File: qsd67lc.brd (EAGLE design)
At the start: 71.1 x 100 mm, 67 parts, among them CON1 RIA-AKL-230-04, CON2 RIA-AKL-230-04, CON3 RIA-AKL-230-03, IC1 MEGA8-P, IC2 BTS555E3146, IC3 MAX3232CPE, IC4 LM2576S, IC5 FT232RL, IC6 ISO7221A, Q1 16MHz, T1 BCR141, U1 HC_05, X2 RS232

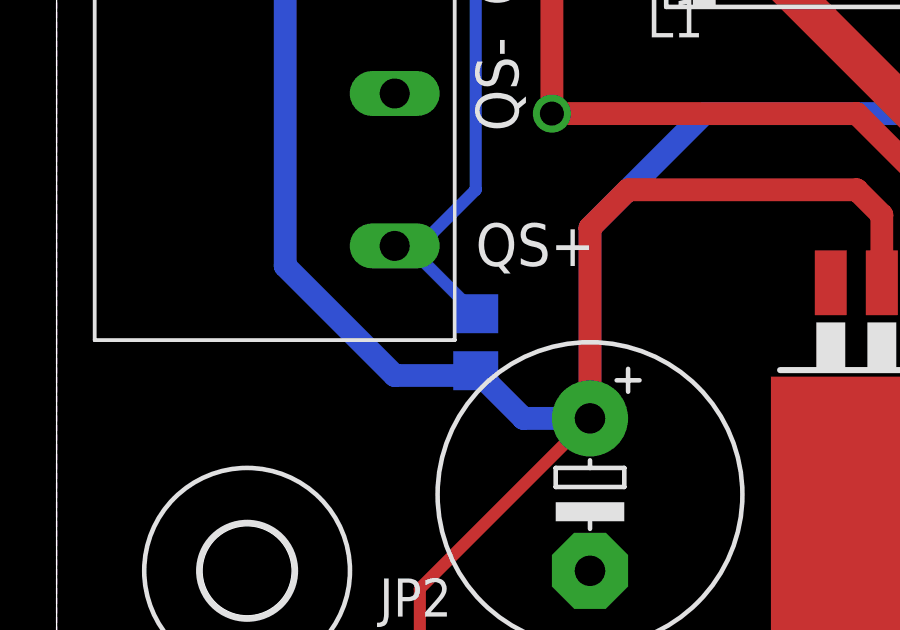
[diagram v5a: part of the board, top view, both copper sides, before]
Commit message: removed doubled pullup resistor for QS+ (R14)
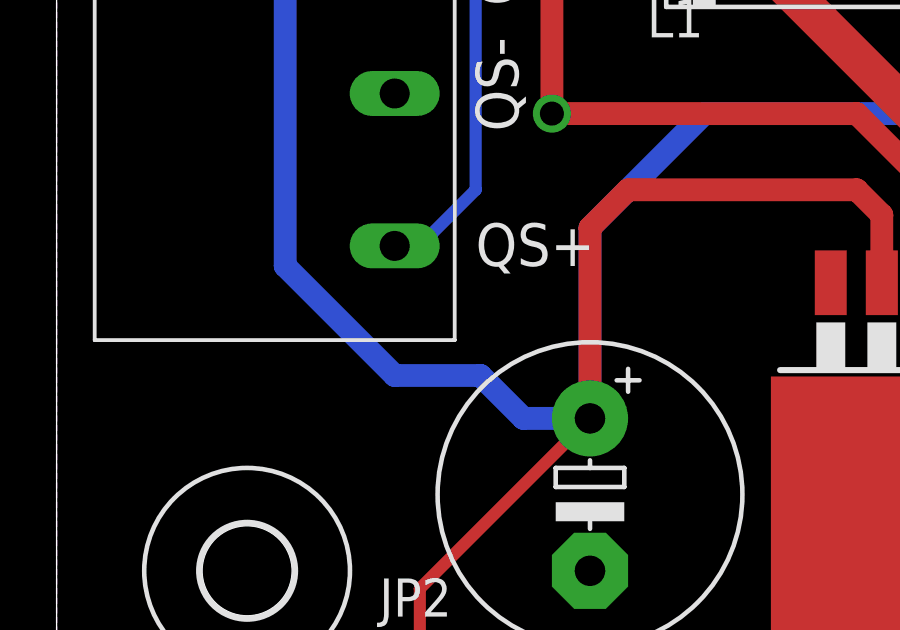
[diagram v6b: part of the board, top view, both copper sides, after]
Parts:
- removed R14: 10k, rcl:R0805
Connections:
- net +3V3: no longer R14.2
- net QS+: no longer R14.1
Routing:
- net QS+: track 40.5 -> 37.3 mm
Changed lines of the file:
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@@
 <?xml version="1.0" encoding="utf-8"?>
 <!DOCTYPE eagle SYSTEM "eagle.dtd">
-<eagle version="9.2.1">
+<eagle version="9.5.0">
 <drawing>
 <settings>
@@
 <attribute name="VALUE" x="69.85" y="13.97" size="1.27" layer="27" rot="R90"/>
 </element>
-<element name="R14" library="rcl" library_urn="urn:adsk.eagle:library:334" package="R0805" package3d_urn="urn:adsk.eagle:package:23553/2" value="10k" x="13.97" y="13.97" smashed="yes" rot="MR270">
-<attribute name="NAME" x="12.7" y="14.605" size="1.27" layer="26" rot="MR270"/>
-<attribute name="SPICEPREFIX" value="R" x="13.97" y="13.97" size="1.778" layer="28" rot="MR270" display="off"/>
-<attribute name="VALUE" x="16.51" y="14.605" size="1.27" layer="28" rot="MR270"/>
-</element>
 <element name="C19" library="rcl" library_urn="urn:adsk.eagle:library:334" package="C0805" package3d_urn="urn:adsk.eagle:package:23617/2" value="100nF" x="36.83" y="41.91" smashed="yes" rot="MR90">
 <attribute name="NAME" x="38.1" y="40.64" size="1.27" layer="26" rot="MR90"/>
@@
 <contactref element="JP4" pad="1"/>
 <contactref element="CON3" pad="P$2"/>
-<wire x1="65.07" y1="70.9" x2="67.31" y2="93.66" width="0" layer="19" extent="1-1"/>
-<wire x1="63.82" y1="69.15" x2="65.07" y2="70.9" width="0" layer="19" extent="1-1"/>
-<wire x1="56.2" y1="66.04" x2="63.82" y2="69.15" width="0" layer="19" extent="1-1"/>
-<wire x1="53.34" y1="66.04" x2="56.2" y2="66.04" width="0" layer="19" extent="1-1"/>
-<wire x1="53.34" y1="63.5" x2="53.34" y2="66.04" width="0" layer="19" extent="1-1"/>
-<wire x1="56.2" y1="62.23" x2="53.34" y2="63.5" width="0" layer="19" extent="1-1"/>
-<wire x1="52.07" y1="70.9" x2="53.34" y2="66.04" width="0" layer="19" extent="1-1"/>
-<wire x1="48.26" y1="70.17" x2="52.07" y2="70.9" width="0" layer="19" extent="1-1"/>
-<wire x1="36.51" y1="76.2" x2="48.26" y2="70.17" width="0" layer="19" extent="1-16"/>
-<wire x1="35.9664" y1="86.36" x2="36.51" y2="76.2" width="0" layer="19" extent="16-16"/>
-<wire x1="24.9936" y1="86.36" x2="35.9664" y2="86.36" width="0" layer="19" extent="1-1"/>
-<wire x1="24.13" y1="81.28" x2="24.9936" y2="86.36" width="0" layer="19" extent="1-1"/>
-<wire x1="25.08" y1="78.74" x2="24.13" y2="81.28" width="0" layer="19" extent="16-16"/>
-<wire x1="21.91" y1="71.12" x2="25.08" y2="78.74" width="0" layer="19" extent="1-16"/>
-<wire x1="27.94" y1="66.04" x2="21.91" y2="71.12" width="0" layer="19" extent="1-16"/>
-<wire x1="58.42" y1="45.72" x2="56.2" y2="62.23" width="0" layer="19" extent="1-1"/>
-<wire x1="58.42" y1="43.815" x2="58.42" y2="45.72" width="0" layer="19" extent="1-1"/>
-<wire x1="64.77" y1="31.75" x2="58.42" y2="43.815" width="0" layer="19" extent="1-1"/>
-<wire x1="46.67" y1="35.56" x2="58.42" y2="43.815" width="0" layer="19" extent="16-16"/>
-<wire x1="39.69" y1="35.56" x2="46.67" y2="35.56" width="0" layer="19" extent="16-16"/>
-<wire x1="39.37" y1="38.1" x2="39.69" y2="35.56" width="0" layer="19" extent="16-16"/>
-<wire x1="36.83" y1="42.86" x2="39.37" y2="38.1" width="0" layer="19" extent="16-16"/>
-<wire x1="36.83" y1="45.72" x2="36.83" y2="42.86" width="0" layer="19" extent="16-16"/>
-<wire x1="33.02" y1="33.34" x2="39.69" y2="35.56" width="0" layer="19" extent="16-16"/>
-<wire x1="33.02" y1="27.94" x2="33.02" y2="33.34" width="0" layer="19" extent="16-16"/>
-<wire x1="25.4" y1="34.29" x2="33.02" y2="33.34" width="0" layer="19" extent="16-16"/>
-<wire x1="18.1" y1="35.56" x2="25.4" y2="34.29" width="0" layer="19" extent="16-16"/>
-<wire x1="19.37" y1="40.64" x2="18.1" y2="35.56" width="0" layer="19" extent="16-16"/>
-<wire x1="11.27" y1="27.34" x2="18.1" y2="35.56" width="0" layer="19" extent="16-16"/>
-<wire x1="11.27" y1="22.26" x2="11.27" y2="27.34" width="0" layer="19" extent="1-1"/>
-<wire x1="40.64" y1="20.32" x2="33.02" y2="27.94" width="0" layer="19" extent="1-1"/>
-<wire x1="43.18" y1="11.43" x2="40.64" y2="20.32" width="0" layer="19" extent="1-1"/>
-<wire x1="39.37" y1="4.13" x2="43.18" y2="11.43" width="0" layer="19" extent="16-16"/>
-<wire x1="2.54" y1="35.56" x2="11.27" y2="27.34" width="0" layer="19" extent="1-1"/>
-<wire x1="29.21" y1="15.9512" x2="40.64" y2="20.32" width="0" layer="19" extent="1-1"/>
-<wire x1="25.8064" y1="15.9512" x2="29.21" y2="15.9512" width="0" layer="19" extent="1-1"/>
-<wire x1="17.78" y1="6.35" x2="25.8064" y2="15.9512" width="0" layer="19" extent="1-1"/>
 </signal>
 <signal name="RXD">
@@
 <wire x1="48.26" y1="72.07" x2="48.59" y2="72.4" width="0.4064" layer="1"/>
 <wire x1="48.59" y1="72.4" x2="52.07" y2="72.4" width="0.4064" layer="1"/>
-<contactref element="R14" pad="2"/>
-<wire x1="13.97" y1="13.02" x2="14.13" y2="12.86" width="0.4064" layer="16"/>
 <wire x1="14.13" y1="12.86" x2="15.56" y2="11.43" width="0.762" layer="16"/>
 <wire x1="15.56" y1="11.43" x2="17.78" y2="11.43" width="0.762" layer="16"/>
@@
 <contactref element="CON3" pad="P$3"/>
 <wire x1="29.21" y1="40.96" x2="29.21" y2="38.1" width="0.4064" layer="16"/>
-<contactref element="R14" pad="1"/>
 <wire x1="21.59" y1="33.02" x2="24.13" y2="35.56" width="0.4064" layer="16"/>
 <wire x1="24.13" y1="35.56" x2="27.94" y2="35.56" width="0.4064" layer="16"/>
@@
 <wire x1="12.1" y1="17.18" x2="11.27" y2="17.18" width="0.4064" layer="16"/>
 <wire x1="16.51" y1="33.02" x2="13.97" y2="30.48" width="0.4064" layer="16"/>
-<wire x1="13.97" y1="14.92" x2="11.71" y2="17.18" width="0.4064" layer="16"/>
 <wire x1="11.71" y1="17.18" x2="11.27" y2="17.18" width="0.4064" layer="16"/>
 </signal>
@@
 <mfgpreviewcolor name="substratecolor" color="0xFF786E46"/>
 </mfgpreviewcolors>
+<errors>
+</errors>
 </board>
 </drawing>
